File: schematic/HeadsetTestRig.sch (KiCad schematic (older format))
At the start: 41 parts, among them J1 Photocell Connector, J2 Programmer Connector, J3 Servo Connector, U1 LD1117S50TR_SOT223, U2 FE1.1s, U3 STM32L432KCUx, Y1 12MHz Crystal, Y2 Crystal

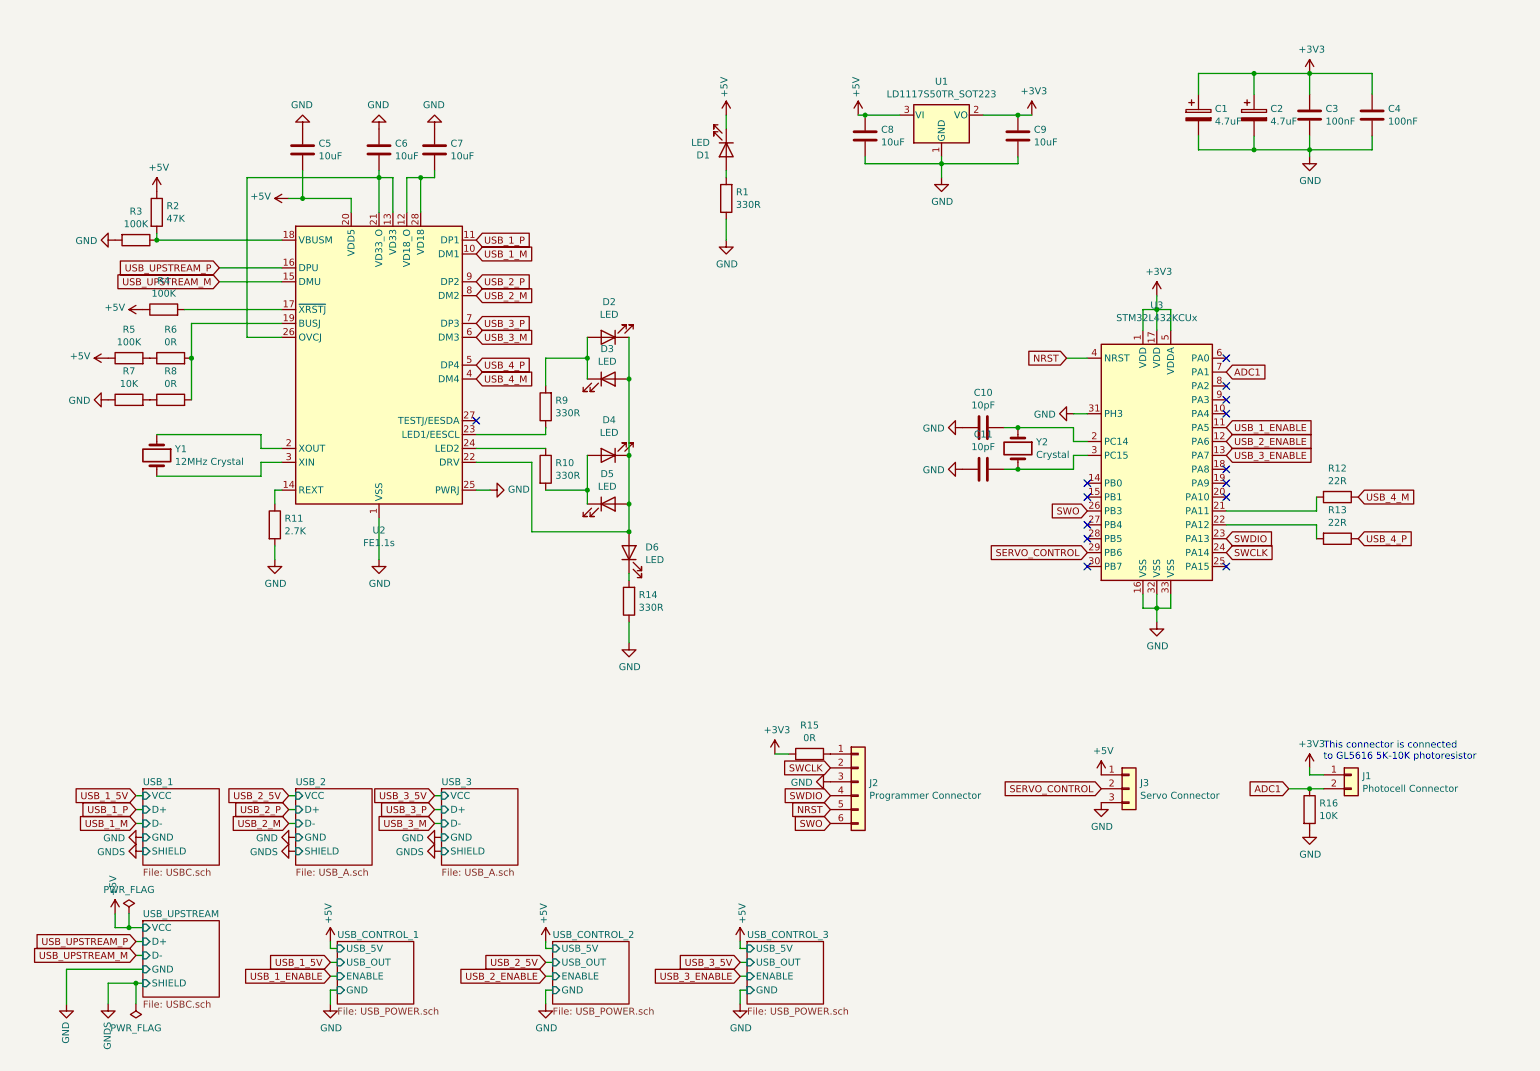
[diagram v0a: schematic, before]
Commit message: Add board, update schematic
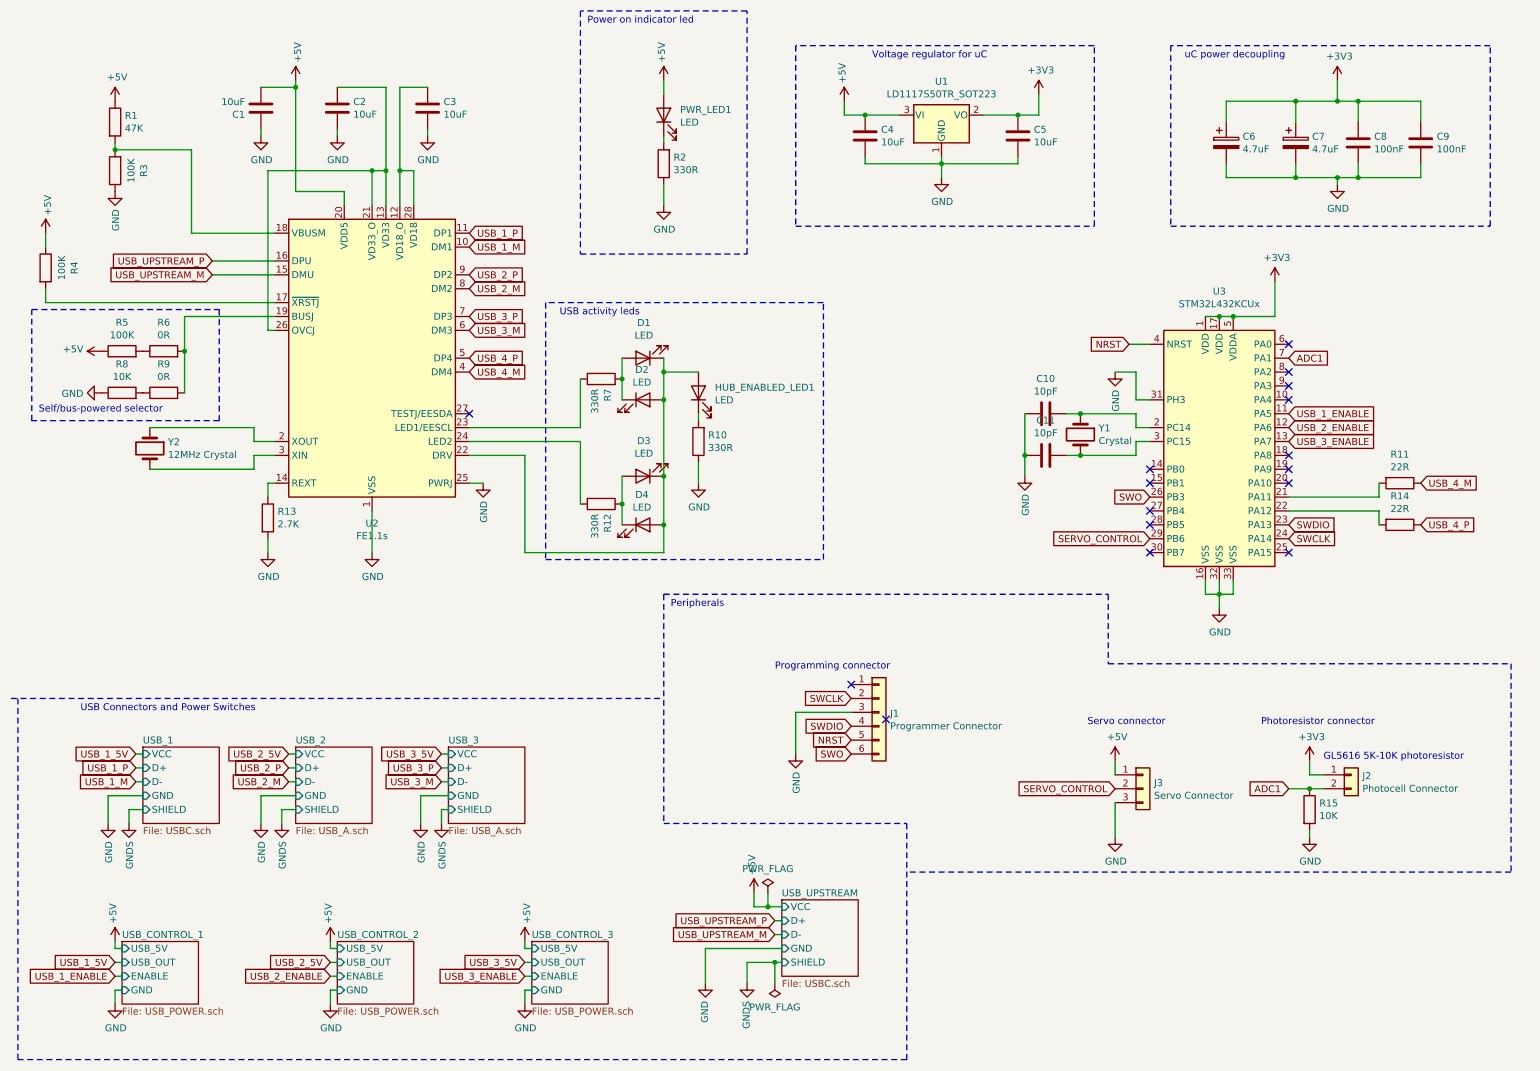
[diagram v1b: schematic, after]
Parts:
- removed R15: 0R, Resistor_SMD:R_0805_2012Metric, symbol Device:R
- J1: renamed from J2; footprint (none) -> Connector_PinHeader_2.54mm:PinHeader_1x06_P2.54mm_Vertical
- J2: renamed from J1; footprint (none) -> Connector_JST:JST_PH_B2B-PH-K_1x02_P2.00mm_Vertical
- J3: footprint (none) -> Connector_JST:JST_PH_B3B-PH-K_1x03_P2.00mm_Vertical
- Y1: renamed from Y2; footprint (none) -> Crystal:Crystal_HC49-U_Vertical
- Y2: renamed from Y1; footprint (none) -> Crystal:Crystal_HC49-U_Vertical
- renumbered C5 to C1, C6 to C2, C7 to C3, C8 to C4, C9 to C5, C1 to C6, C2 to C7, C3 to C8, C4 to C9, D2 to D1, D3 to D2, D4 to D3, D5 to D4, D6 to HUB_ENABLED_LED1, D1 to PWR_LED1, R2 to R1, R14 to R10, R12 to R11, R10 to R12, R11 to R13, R13 to R14, R16 to R15, R1 to R2, R9 to R7, R7 to R8, R8 to R9
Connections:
- net +5V: now also PWR_LED1.2 (A); no longer PWR_LED1.1 (K)
- net GND: now also C2.2, C3.2, R3.1; no longer C2.1, C3.1, R3.2
- net at U2.12 (VD18_O), U2.28 (VD18): now also C3.1; no longer C3.2
- net at U2.13 (VD33), U2.21 (VD33_O), U2.26 (OVCJ): now also C2.1; no longer C2.2
- net at R1.2, U2.18 (VBUSM): now also R3.2; no longer R3.1
- net at U2.24 (LED2): now also R12.2; no longer R12.1
- net at R2.2: now also PWR_LED1.1 (K); no longer PWR_LED1.2 (A)
- net at D3.2 (A), D4.1 (K): now also R12.1; no longer R12.2
- no-connect marks 14 -> 16
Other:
- note added: "GL5616 5K-10K photoresistor"
- note added: "Peripherals"
- note added: "Photoresistor connector"
- note added: "Power on indicator led"
- note added: "Programming connector"
- note added: "Self/bus-powered selector"
- note added: "Servo connector"
- note added: "USB Connectors and Power Switches"
- note added: "USB activity leds"
- note added: "Voltage regulator for uC"
- note added: "uC power decoupling"
- note removed: "This connector is connected \nto GL5616 5K-10K photoresistor"
- moved on the sheet: C1, C10, C11, C2, C3, C6, C7, C8, C9, D1, D2, D3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
